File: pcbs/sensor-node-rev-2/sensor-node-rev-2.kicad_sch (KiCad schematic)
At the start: 75 parts, among them IC1 NPP-301A-700AT, IC2 AD8226ARMZ, J2 DEBUG_CONN, J3 SMA EDGE CONN, J4 UART_CONN, U1 STM32U031K8U6, U2 nRF24L01P, U4 TLV9001IDCK, Y1 Crystal_16MHz

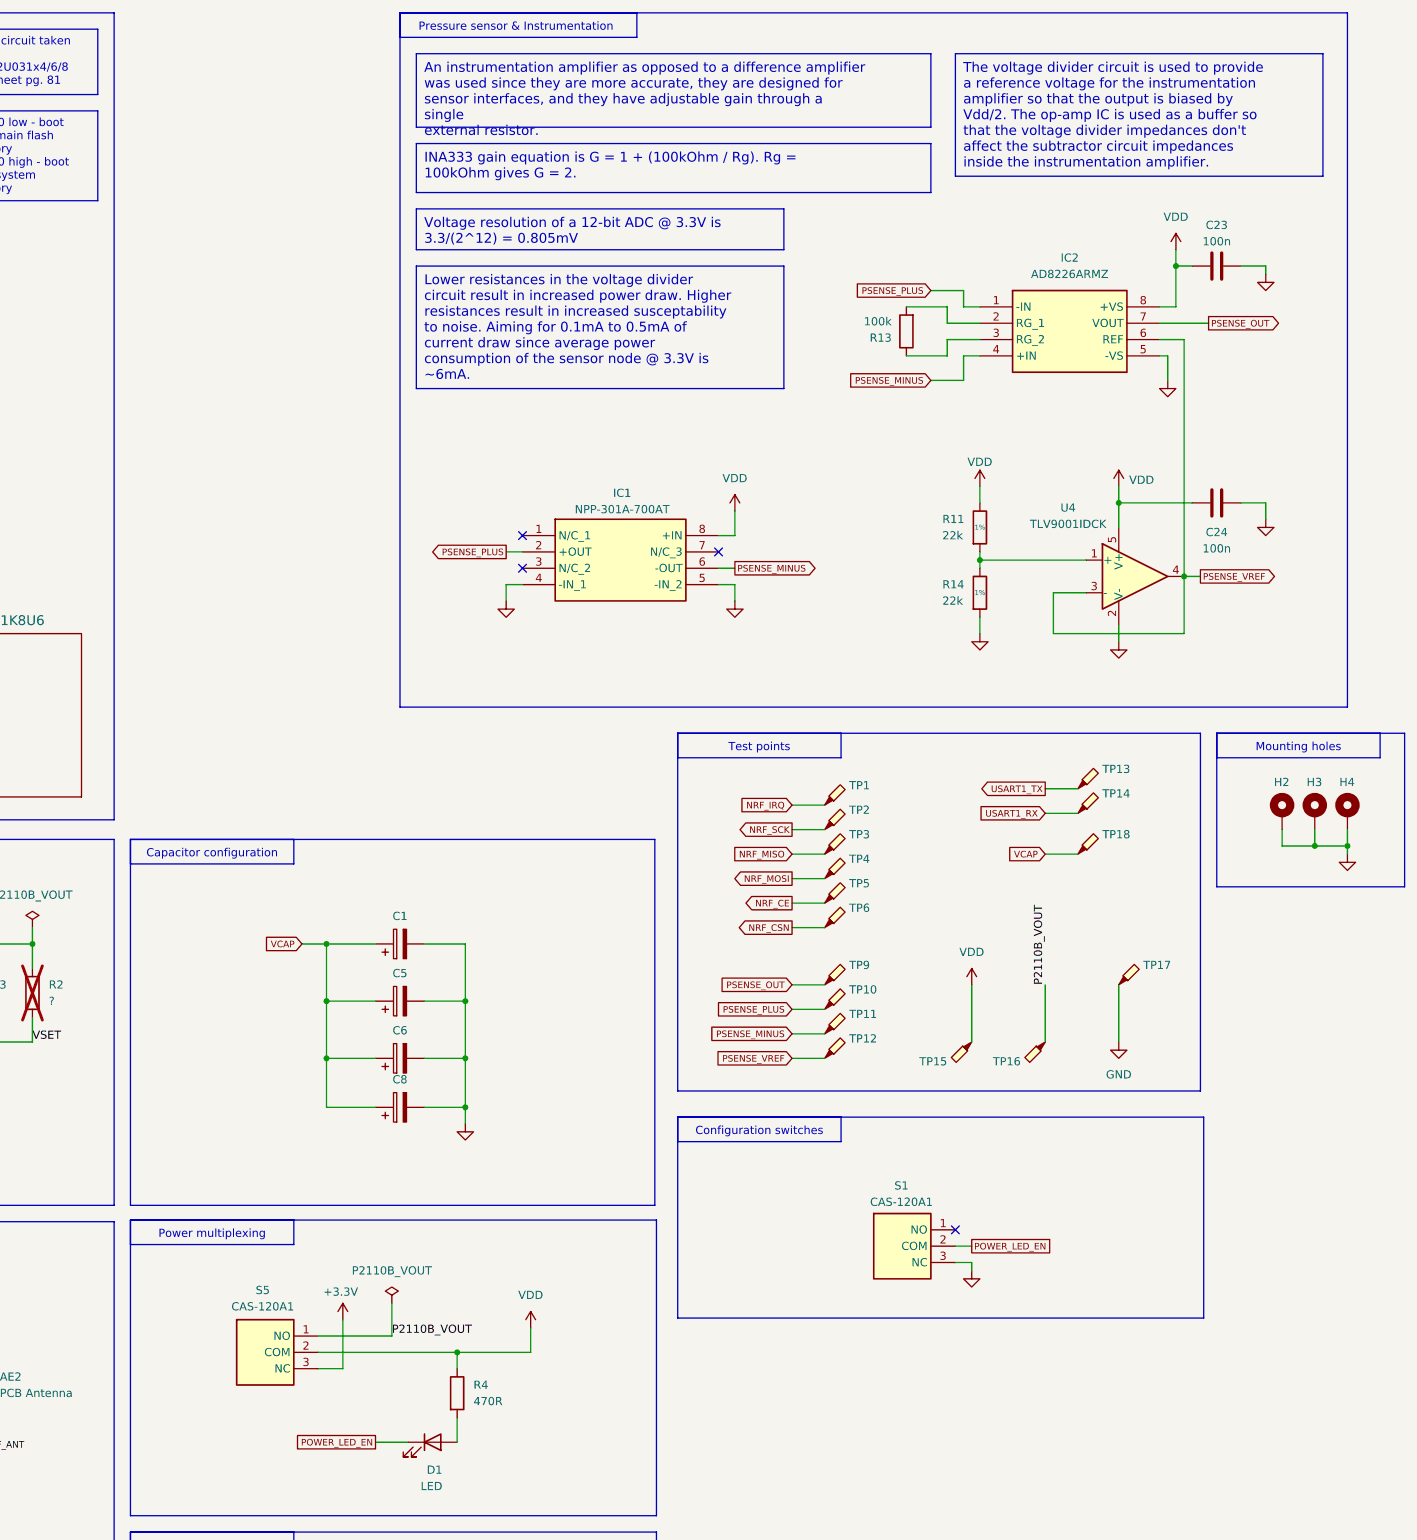
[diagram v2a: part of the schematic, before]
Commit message: Add footprint and back silkscreen
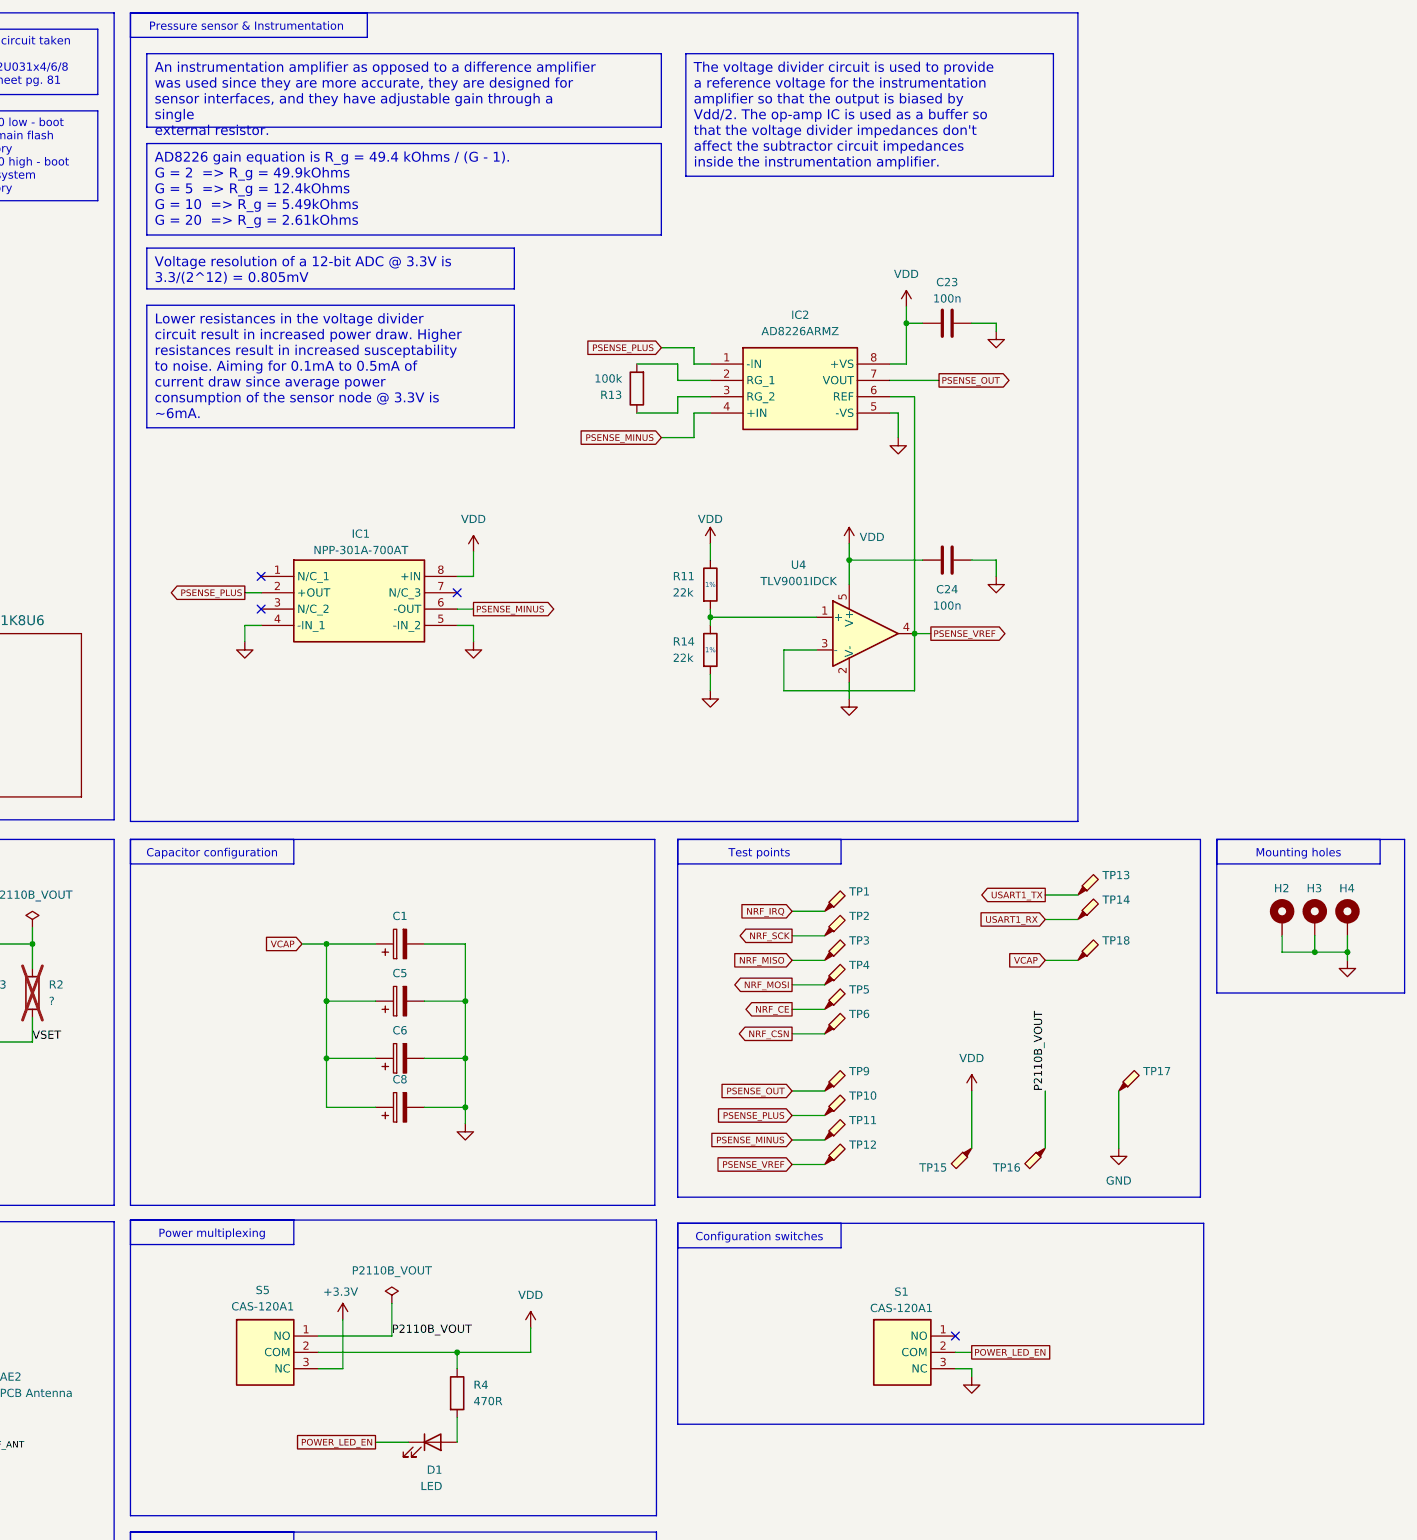
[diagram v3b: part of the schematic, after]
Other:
- moved on the sheet: C23, C24, H2, H3, H4, IC1, IC2, R11, R13, R14, S1, TP1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

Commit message: Add BOM and initial manufacturing files
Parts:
- added R12: 5.49k, Resistor_SMD:R_0402_1005Metric, symbol Device:R
- added R15: 2.61k, Resistor_SMD:R_0402_1005Metric, symbol Device:R
- added R9: 12.4k, Resistor_SMD:R_0402_1005Metric, symbol Device:R
- AE2, R2: now left out of the parts list
- C1, C5, C6, C8: Manufacturer_Part_Number F720J108MMCAQ2 -> T520D108M2R5ATE030; Mouser Part Number 581-F720J108MMCAQ2 -> 80-T520D108M2R5ATE30
- C10, C12: Manufacturer_Part_Number 0402ZA120JAT2A -> GRM1555C1E120GA01D; Mouser Part Number 581-0402ZA120JAT2A -> 81-GCM1555G1H120GA6J
- C13: Manufacturer_Part_Number 04026C102JAT2A -> GRM1555C1H102GA01D; Mouser Part Number 581-04026C102JAT2A -> 81-GRM1555C1H102GA1D
- C14: Manufacturer_Part_Number 0402ZD103MAT2A -> GRM155R71H103JA88D; Mouser Part Number 581-0402ZD103MAT2A -> 81-GRM155R71H103JA8D
- C17: Manufacturer_Part_Number 0402ZC222KAT2A -> GRM155R71H222JA01D; Mouser Part Number 581-0402ZC222KAT2A -> 81-GRM36X222J50
- C18: Manufacturer_Part_Number 04026A4R7BAT2A -> GCM1555C1H4R7BA16J; Mouser Part Number 581-04026A4R7BAT2A -> 81-GCM1555C1H4R7BA6J
- C2, C22, C23, C24, C3, C4: Manufacturer_Part_Number 0402X7R104KT7AT -> GRM155R61E104KA87J; Mouser Part Number 581-0402X7R104KT7AT -> 81-GRM155R61E104KA7J
- J3: Manufacturer_Part_Number 73251-1150 -> EMPCB.SMAFSTJ.B.HT; Mouser Part Number 538-73251-1150 -> 960-EMPCB.SMAFSTJBHT
- R13: value 100k -> 49.9k; Manufacturer_Part_Number ERJ-U02J104X -> ERJ-2RKF4992X; Mouser Part Number 667-ERJ-U02J104X -> 667-ERJ-2RKF4992X
- R3: value ? -> 4.3M; Manufacturer_Part_Number (none) -> CRCW04024M32FKED; Mouser Part Number (none) -> 71-CRCW04024M32FKED
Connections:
- net at IC2.2 (RG_1), R13.2: now also R12.2, R15.2, R9.2
- net at IC2.3 (RG_2), R13.1: now also R12.1, R15.1, R9.1
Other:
- moved on the sheet: C23, C24, IC2, R11, R13, R14, U4

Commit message: Update BOM with better tolerance capacitor
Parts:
- C9: Manufacturer_Part_Number GRM155R61A333MA01J -> GRM155R71H333KE14J; Mouser Part Number 81-GRM155R61A333MA1J -> 81-GRM155R71H333KE4J
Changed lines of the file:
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@@
 			)
 		)
-		(property "Manufacturer_Part_Number" "GRM155R61A333MA01J"
+		(property "Manufacturer_Part_Number" "GRM155R71H333KE14J"
 			(at 43.18 257.81 0)
 			(effects
@@
 			)
 		)
-		(property "Mouser Part Number" "81-GRM155R61A333MA1J"
+		(property "Mouser Part Number" " 81-GRM155R71H333KE4J "
 			(at 43.18 257.81 0)
 			(effects

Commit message: Update manufacturing files and BOM to account for different SMA connector
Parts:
- C10, C12: Manufacturer_Part_Number GRM1555C1E120GA01D -> GCM1555G1H120GA16J
- J3: Manufacturer_Part_Number EMPCB.SMAFSTJ.B.HT -> 901-10309; Mouser Part Number 960-EMPCB.SMAFSTJBHT -> 523-901-10309
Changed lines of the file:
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@@
 			)
 		)
-		(property "Manufacturer_Part_Number" " EMPCB.SMAFSTJ.B.HT "
+		(property "Manufacturer_Part_Number" " 901-10309 "
 			(at 43.18 168.91 0)
 			(effects
@@
 			)
 		)
-		(property "Mouser Part Number" " 960-EMPCB.SMAFSTJBHT "
+		(property "Mouser Part Number" "523-901-10309 "
 			(at 43.18 168.91 0)
 			(effects
@@
 			)
 		)
-		(property "Manufacturer_Part_Number" "GRM1555C1E120GA01D"
+		(property "Manufacturer_Part_Number" "GCM1555G1H120GA16J"
 			(at 109.22 269.24 0)
 			(effects
@@
 			)
 		)
-		(property "Manufacturer_Part_Number" "GRM1555C1E120GA01D"
+		(property "Manufacturer_Part_Number" "GCM1555G1H120GA16J"
 			(at 86.36 269.24 0)
 			(effects
